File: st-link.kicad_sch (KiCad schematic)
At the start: 34 parts, among them J401 Conn_01x06_Pin, Q700 MMST3904, U700 STM32F103CBTx, Y700 8 MHz

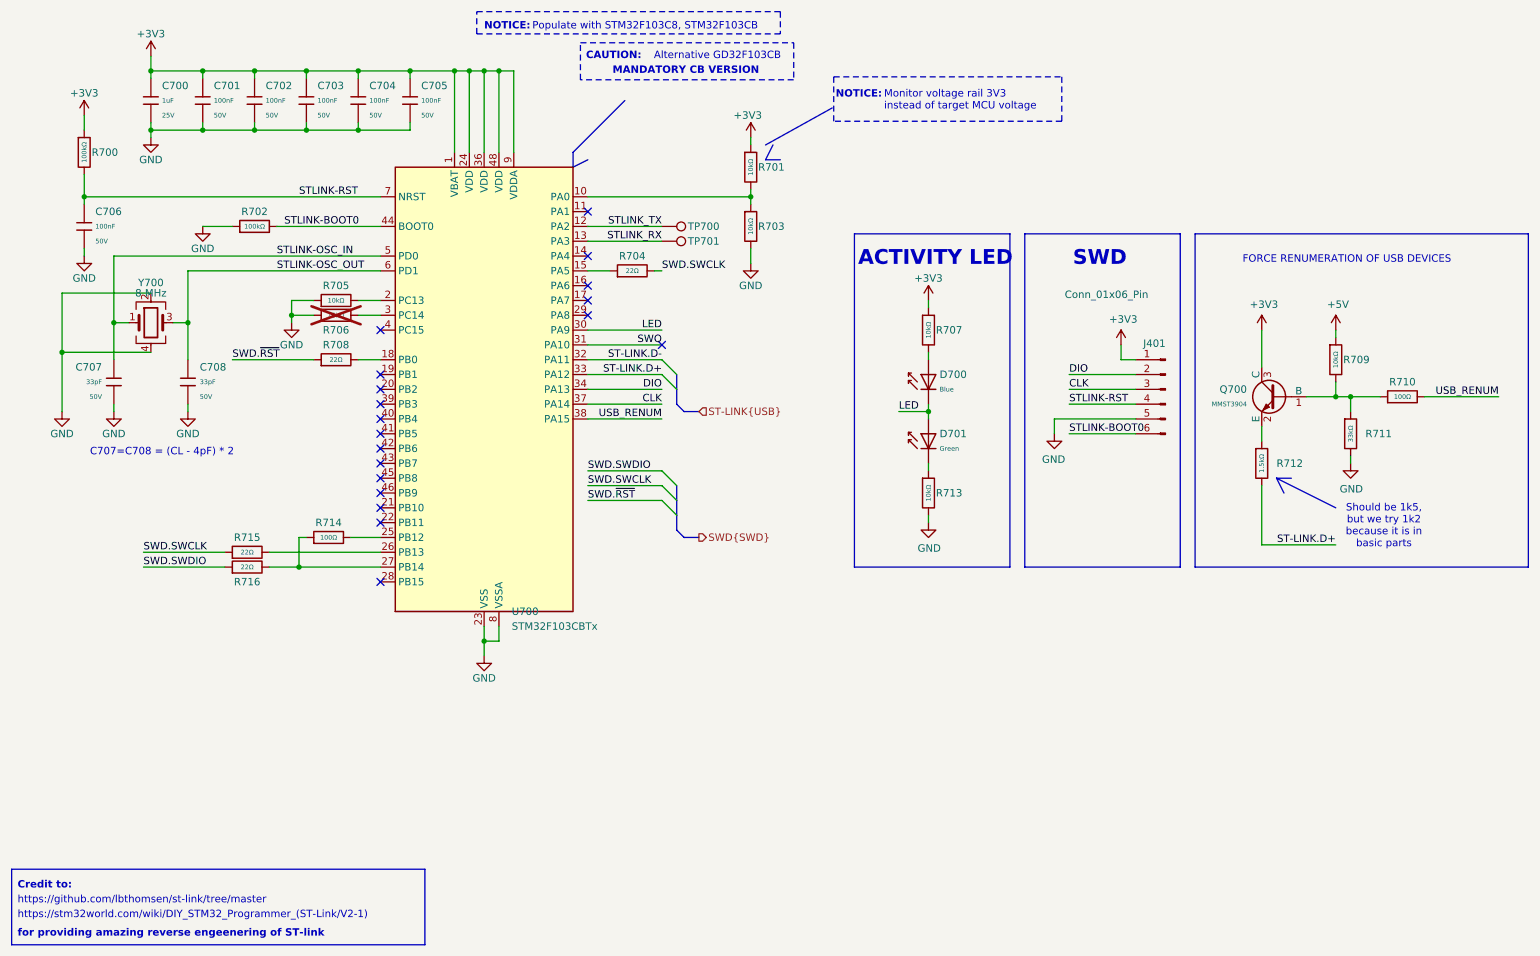
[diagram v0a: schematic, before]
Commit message: Change MCU to STM32H563
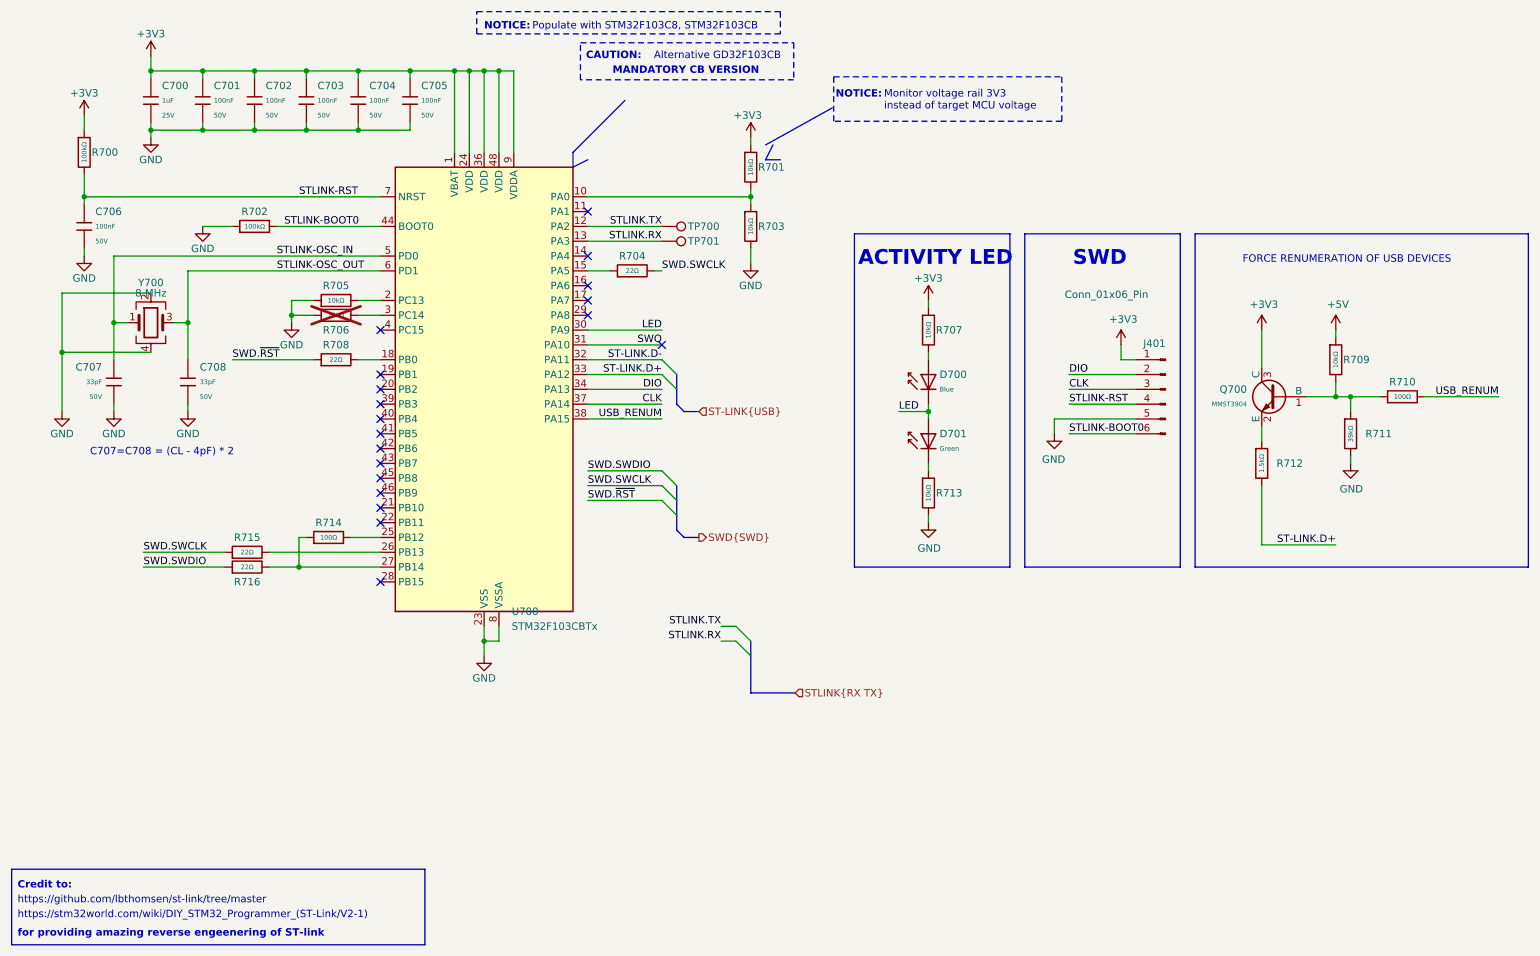
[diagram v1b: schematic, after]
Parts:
- removed R711: 33kΩ, PCM_JLCPCB:R_0402, symbol PCM_JLCPCB-Resistors:0402,33kΩ
- added R711: 39kΩ, PCM_JLCPCB:R_0402, symbol PCM_JLCPCB-Resistors:0402,39kΩ
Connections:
- net GND: now also R711.2
- net at Q700.1 (B), R709.2, R710.1: now also R711.1
- net STLINK_RX renamed STLINK.RX
- net STLINK_TX renamed STLINK.TX
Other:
- note removed: "Should be 1k5, but we try 1k2 because it is in basic parts"

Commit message: Add LCSC numbers
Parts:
- removed R711: 39kΩ, PCM_JLCPCB:R_0402, symbol PCM_JLCPCB-Resistors:0402,39kΩ
- added R404: 36kΩ, PCM_JLCPCB:R_0603, symbol PCM_JLCPCB-Resistors:0603,36kΩ
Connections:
- net GND: now also R404.2
- net at Q700.1 (B), R709.2, R710.1: now also R404.1
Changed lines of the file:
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@@
+	)
+	(symbol
+		(lib_id "PCM_JLCPCB-Resistors:0603,36kΩ")
+		(at 245.11 106.68 0)
+		(unit 1)
+		(exclude_from_sim no)
+		(in_bom yes)
+		(on_board yes)
+		(dnp no)
+		(fields_autoplaced yes)
+		(property "Reference" "R404"
+			(at 247.65 106.6799 0)
+			(effects
+				(font
+					(size 1.27 1.27)
+				)
+				(justify left)
+			)
+		)
+		(property "Value" "36kΩ"
+			(at 245.11 106.68 90)
+			(do_not_autoplace yes)
+			(effects
+				(font
+					(size 0.8 0.8)
+				)
+			)
+		)
+		(property "Footprint" "PCM_JLCPCB:R_0603"
+			(at 243.332 106.68 90)
+			(effects
+				(font
+					(size 1.27 1.27)
+				)
+				(hide yes)
+			)
+		)
+		(property "Datasheet" "https://www.lcsc.com/datasheet/lcsc_datasheet_2206010116_UNI-ROYAL-Uniroyal-Elec-0603WAF3602T5E_C23147.pdf"
+			(at 245.11 106.68 0)
+			(effects
+				(font
+					(size 1.27 1.27)
+				)
+				(hide yes)
+			)
+		)
+		(property "Description" "100mW Thick Film Resistors 75V ±100ppm/°C ±1% 36kΩ 0603 Chip Resistor - Surface Mount ROHS"
+			(at 245.11 106.68 0)
+			(effects
+				(font
+					(size 1.27 1.27)
+				)
+				(hide yes)
+			)
+		)
+		(property "LCSC" "C23147"
+			(at 245.11 106.68 0)
+			(effects
+				(font
+					(size 1.27 1.27)
+				)
+				(hide yes)
+			)
+		)
+		(property "Stock" "258935"
+			(at 245.11 106.68 0)
+			(effects
+				(font
+					(size 1.27 1.27)
+				)
+				(hide yes)
+			)
+		)
+		(property "Price" "0.004USD"
+			(at 245.11 106.68 0)
+			(effects
+				(font
+					(size 1.27 1.27)
+				)
+				(hide yes)
+			)
+		)
+		(property "Process" "SMT"
+			(at 245.11 106.68 0)
+			(effects
+				(font
+					(size 1.27 1.27)
+				)
+				(hide yes)
+			)
+		)
+		(property "Minimum Qty" "20"
+			(at 245.11 106.68 0)
+			(effects
+				(font
+					(size 1.27 1.27)
+				)
+				(hide yes)
+			)
+		)
+		(property "Attrition Qty" "10"
+			(at 245.11 106.68 0)
+			(effects
+				(font
+					(size 1.27 1.27)
+				)
+				(hide yes)
+			)
+		)
+		(property "Class" "Preferred Component"
+			(at 245.11 106.68 0)
+			(effects
+				(font
+					(size 1.27 1.27)
+				)
+				(hide yes)
+			)
+		)
+		(property "Category" "Resistors,Chip Resistor - Surface Mount"
+			(at 245.11 106.68 0)
+			(effects
+				(font
+					(size 1.27 1.27)
+				)
+				(hide yes)
+			)
+		)
+		(property "Manufacturer" "UNI-ROYAL(Uniroyal Elec)"
+			(at 245.11 106.68 0)
+			(effects
+				(font
+					(size 1.27 1.27)
+				)
+				(hide yes)
+			)
+		)
+		(property "Part" "0603WAF3602T5E"
+			(at 245.11 106.68 0)
+			(effects
+				(font
+					(size 1.27 1.27)
+				)
+				(hide yes)
+			)
+		)
+		(property "Resistance" "36kΩ"
+			(at 245.11 106.68 0)
+			(effects
+				(font
+					(size 1.27 1.27)
+				)
+				(hide yes)
+			)
+		)
+		(property "Power(Watts)" "100mW"
+			(at 245.11 106.68 0)
+			(effects
+				(font
+					(size 1.27 1.27)
+				)
+				(hide yes)
+			)
+		)
+		(property "Type" "Thick Film Resistors"
+			(at 245.11 106.68 0)
+			(effects
+				(font
+					(size 1.27 1.27)
+				)
+				(hide yes)
+			)
+		)
+		(property "Overload Voltage (Max)" "75V"
+			(at 245.11 106.68 0)
+			(effects
+				(font
+					(size 1.27 1.27)
+				)
+				(hide yes)
+			)
+		)
+		(property "Operating Temperature Range" "-55°C~+155°C"
+			(at 245.11 106.68 0)
+			(effects
+				(font
+					(size 1.27 1.27)
+				)
+				(hide yes)
+			)
+		)
+		(property "Tolerance" "±1%"
+			(at 245.11 106.68 0)
+			(effects
+				(font
+					(size 1.27 1.27)
+				)
+				(hide yes)
+			)
+		)
+		(property "Temperature Coefficient" "±100ppm/°C"
+			(at 245.11 106.68 0)
+			(effects
+				(font
+					(size 1.27 1.27)
+				)
+				(hide yes)
+			)
+		)
+		(pin "2"
+		)
+		(pin "1"
+		)
+		(instances
+			(project ""
+				(path "/090a8e41-87a8-4fb1-998b-60a2c0dc4cee/ed5910e5-42de-4923-b023-9e23a66937d0"
+					(reference "R404")
+					(unit 1)
+				)
+			)
+		)
 	)
 	(symbol
@@
 					(unit 1)
 				)
-			)
-		)
-	)
-	(symbol
-		(lib_id "PCM_JLCPCB-Resistors:0402,39kΩ")
-		(at 245.11 106.68 0)
-		(unit 1)
-		(exclude_from_sim no)
-		(in_bom yes)
-		(on_board yes)
-		(dnp no)
-		(fields_autoplaced yes)
-		(property "Reference" "R711"
-			(at 247.65 106.6799 0)
-			(effects
-				(font
-					(size 1.27 1.27)
-				)
-				(justify left)
-			)
-		)
-		(property "Value" "39kΩ"
-			(at 245.11 106.68 90)
-			(do_not_autoplace yes)
-			(effects
-				(font
-					(size 0.8 0.8)
-				)
-			)
-		)
-		(property "Footprint" "PCM_JLCPCB:R_0402"
-			(at 243.332 106.68 90)
-			(effects
-				(font
-					(size 1.27 1.27)
-				)
-				(hide yes)
-			)
-		)
-		(property "Datasheet" "https://www.lcsc.com/datasheet/lcsc_datasheet_2206010100_UNI-ROYAL-Uniroyal-Elec-0402WGF3902TCE_C25783.pdf"
-			(at 245.11 106.68 0)
-			(effects
-				(font
-					(size 1.27 1.27)
-				)
-				(hide yes)
-			)
-		)
-		(property "Description" "62.5mW Thick Film Resistors 50V ±100ppm/°C ±1% 39kΩ 0402 Chip Resistor - Surface Mount ROHS"
-			(at 245.11 106.68 0)
-			(effects
-				(font
-					(size 1.27 1.27)
-				)
-				(hide yes)
-			)
-		)
-		(property "LCSC" "C25783"
-			(at 245.11 106.68 0)
-			(effects
-				(font
-					(size 1.27 1.27)
-				)
-				(hide yes)
-			)
-		)
-		(property "Stock" "50927"
-			(at 245.11 106.68 0)
-			(effects
-				(font
-					(size 1.27 1.27)
-				)
-				(hide yes)
-			)
-		)
-		(property "Price" "0.004USD"
-			(at 245.11 106.68 0)
-			(effects
-				(font
-					(size 1.27 1.27)
-				)
-				(hide yes)
-			)
-		)
-		(property "Process" "SMT"
-			(at 245.11 106.68 0)
-			(effects
-				(font
-					(size 1.27 1.27)
-				)
-				(hide yes)
-			)
-		)
-		(property "Minimum Qty" "20"
-			(at 245.11 106.68 0)
-			(effects
-				(font
-					(size 1.27 1.27)
-				)
-				(hide yes)
-			)
-		)
-		(property "Attrition Qty" "10"
-			(at 245.11 106.68 0)
-			(effects
-				(font
-					(size 1.27 1.27)
-				)
-				(hide yes)
-			)
-		)
-		(property "Class" "Preferred Component"
-			(at 245.11 106.68 0)
-			(effects
-				(font
-					(size 1.27 1.27)
-				)
-				(hide yes)
-			)
-		)
-		(property "Category" "Resistors,Chip Resistor - Surface Mount"
-			(at 245.11 106.68 0)
-			(effects
-				(font
-					(size 1.27 1.27)
-				)
-				(hide yes)
-			)
-		)
-		(property "Manufacturer" "UNI-ROYAL(Uniroyal Elec)"
-			(at 245.11 106.68 0)
-			(effects
-				(font
-					(size 1.27 1.27)
-				)
-				(hide yes)
-			)
-		)
-		(property "Part" "0402WGF3902TCE"
-			(at 245.11 106.68 0)
-			(effects
-				(font
-					(size 1.27 1.27)
-				)
-				(hide yes)
-			)
-		)
-		(property "Resistance" "39kΩ"
-			(at 245.11 106.68 0)
-			(effects
-				(font
-					(size 1.27 1.27)
-				)
-				(hide yes)
-			)
-		)
-		(property "Power(Watts)" "62.5mW"
-			(at 245.11 106.68 0)
-			(effects
-				(font
-					(size 1.27 1.27)
-				)
-				(hide yes)
-			)
-		)
-		(property "Type" "Thick Film Resistors"
-			(at 245.11 106.68 0)
-			(effects
-				(font
-					(size 1.27 1.27)
-				)
-				(hide yes)
-			)
-		)
-		(property "Overload Voltage (Max)" "50V"
-			(at 245.11 106.68 0)
-			(effects
-				(font
-					(size 1.27 1.27)
-				)
-				(hide yes)
-			)
-		)
-		(property "Operating Temperature Range" "-55°C~+155°C"
-			(at 245.11 106.68 0)
-			(effects
-				(font
-					(size 1.27 1.27)
-				)
-				(hide yes)
-			)
-		)
-		(property "Tolerance" "±1%"
-			(at 245.11 106.68 0)
-			(effects
-				(font
-					(size 1.27 1.27)
-				)
-				(hide yes)
-			)
-		)
-		(property "Temperature Coefficient" "±100ppm/°C"
-			(at 245.11 106.68 0)
-			(effects
-				(font
-					(size 1.27 1.27)
-				)
-				(hide yes)
-			)
-		)
-		(pin "2"
-		)
-		(pin "1"
-		)
-		(instances
-			(project ""
-				(path "/090a8e41-87a8-4fb1-998b-60a2c0dc4cee/ed5910e5-42de-4923-b023-9e23a66937d0"
-					(reference "R711")
-					(unit 1)
-				)
